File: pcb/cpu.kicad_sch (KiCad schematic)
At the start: 9 parts, among them J9 CLKMUL SET, U1 486Socket

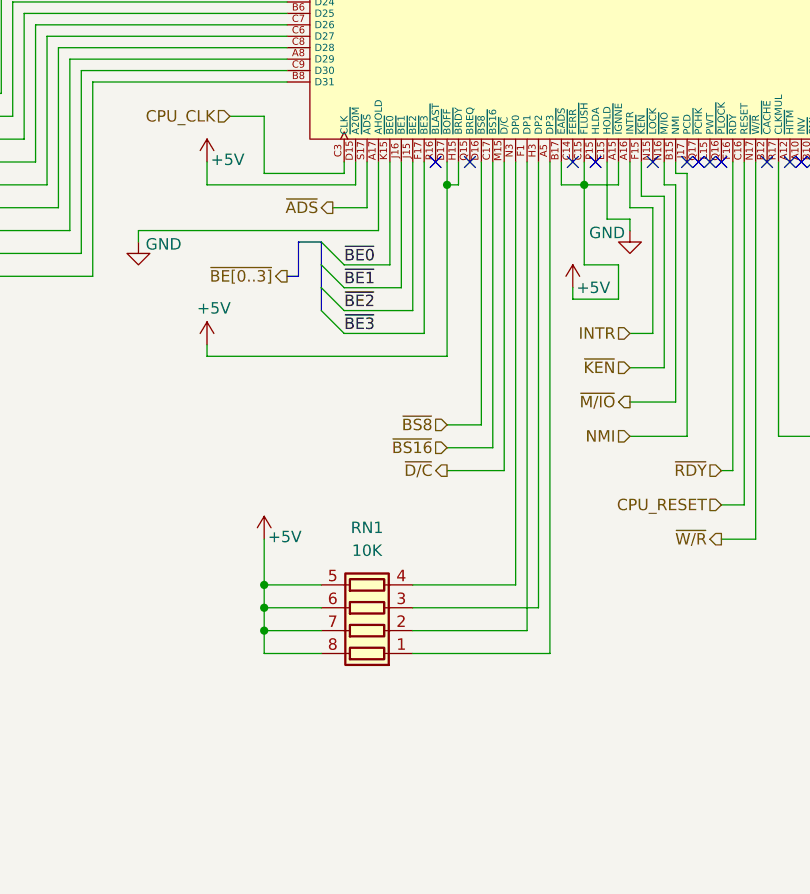
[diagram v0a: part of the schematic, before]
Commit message: reverting 'cpu DPx use Resistor Array instead of individual resistors'
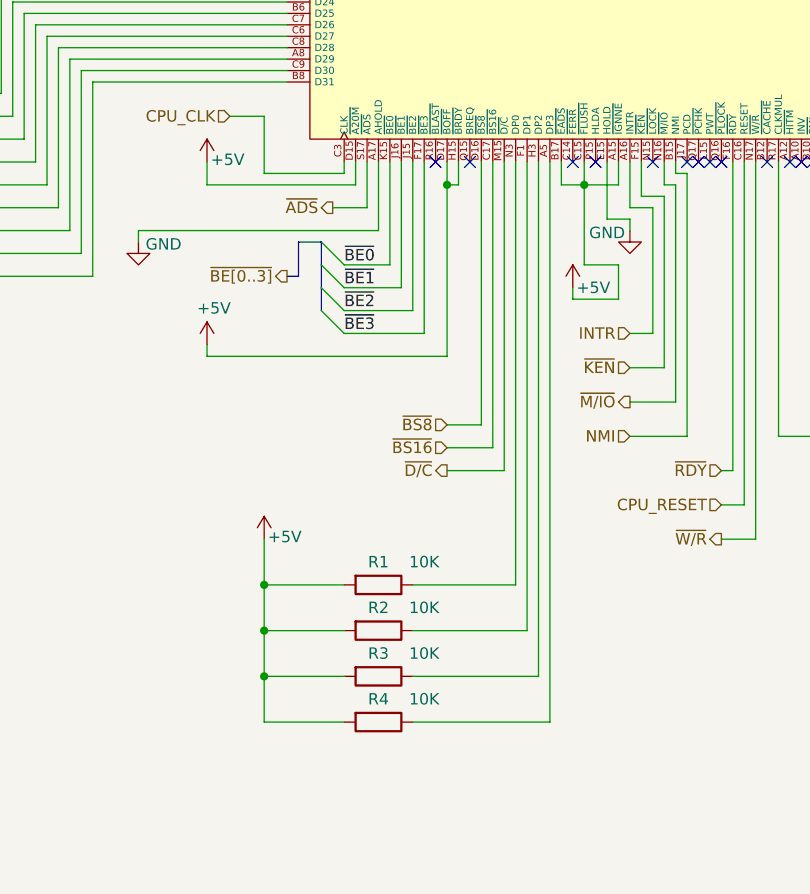
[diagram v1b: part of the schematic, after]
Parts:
- removed RN1: 10K, Resistor_SMD:R_Array_Convex_4x1206, symbol Device:R_Pack04
- added R1, R2, R3, R4: 10K, Resistor_SMD:R_0805_2012Metric_Pad1.20x1.40mm_HandSolder, symbol Device:R
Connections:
- net +5V: now also R1.2, R2.2, R3.2, R4.2
- net at U1.A5 (DP3): now also R4.1
- net at U1.F1 (DP1): now also R2.1
- net at U1.H3 (DP2): now also R3.1
- net at U1.N3 (DP0): now also R1.1

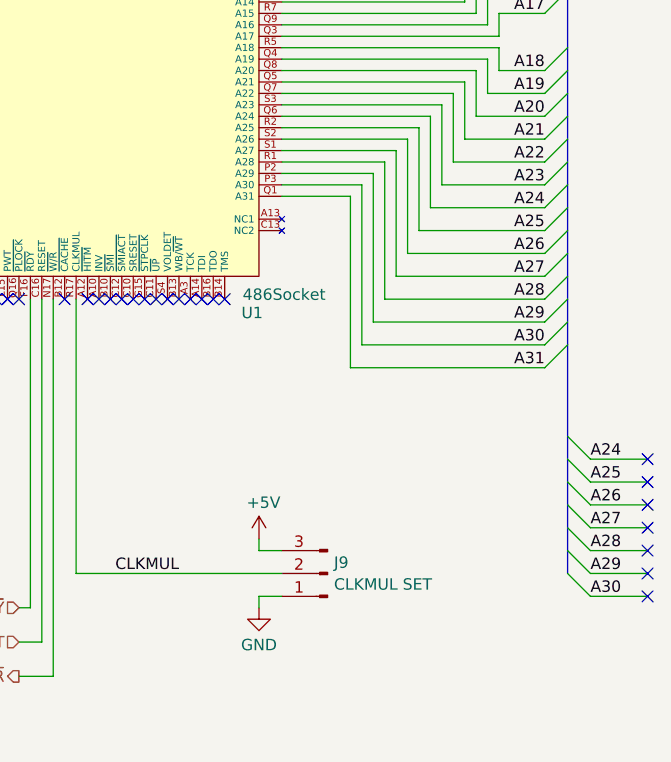
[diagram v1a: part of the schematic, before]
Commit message: reversed BEx/CPU_IN_BE order to reflect PCB layout, 515 VIAs
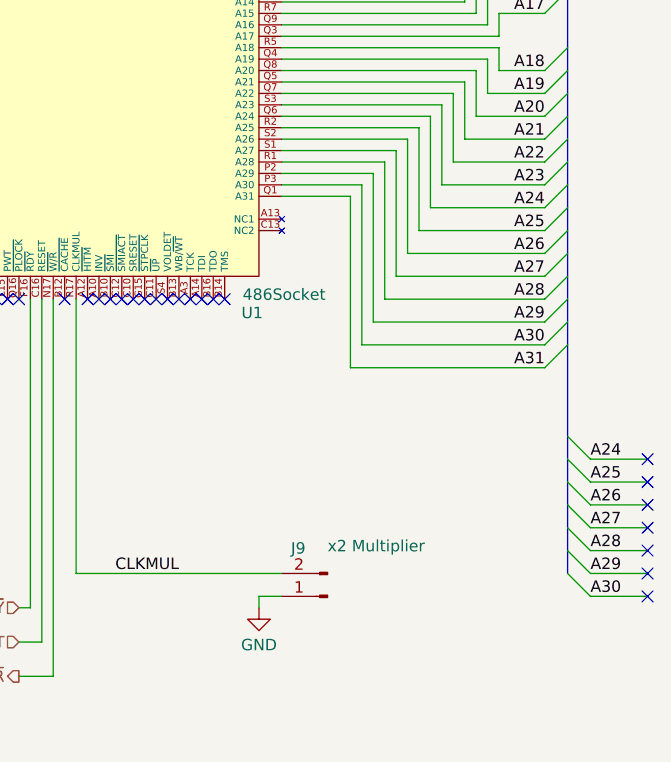
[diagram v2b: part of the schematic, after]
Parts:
- removed J9: CLKMUL SET, Connector_PinHeader_2.54mm:PinHeader_1x03_P2.54mm_Vertical, symbol Connector:Conn_01x03_Pin
- added J9: x2 Multiplier, Connector_PinHeader_2.54mm:PinHeader_1x02_P2.54mm_Vertical, symbol Connector:Conn_01x02_Pin
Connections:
- net CLKMUL: now also J9.2 (Pin_2)
- net GND: now also J9.1 (Pin_1)
